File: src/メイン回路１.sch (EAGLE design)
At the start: 33 parts, among them T1 一般的なトランジスタ, T2 一般的なトランジスタ, T3 一般的なトランジスタ, T4 一般的なトランジスタ

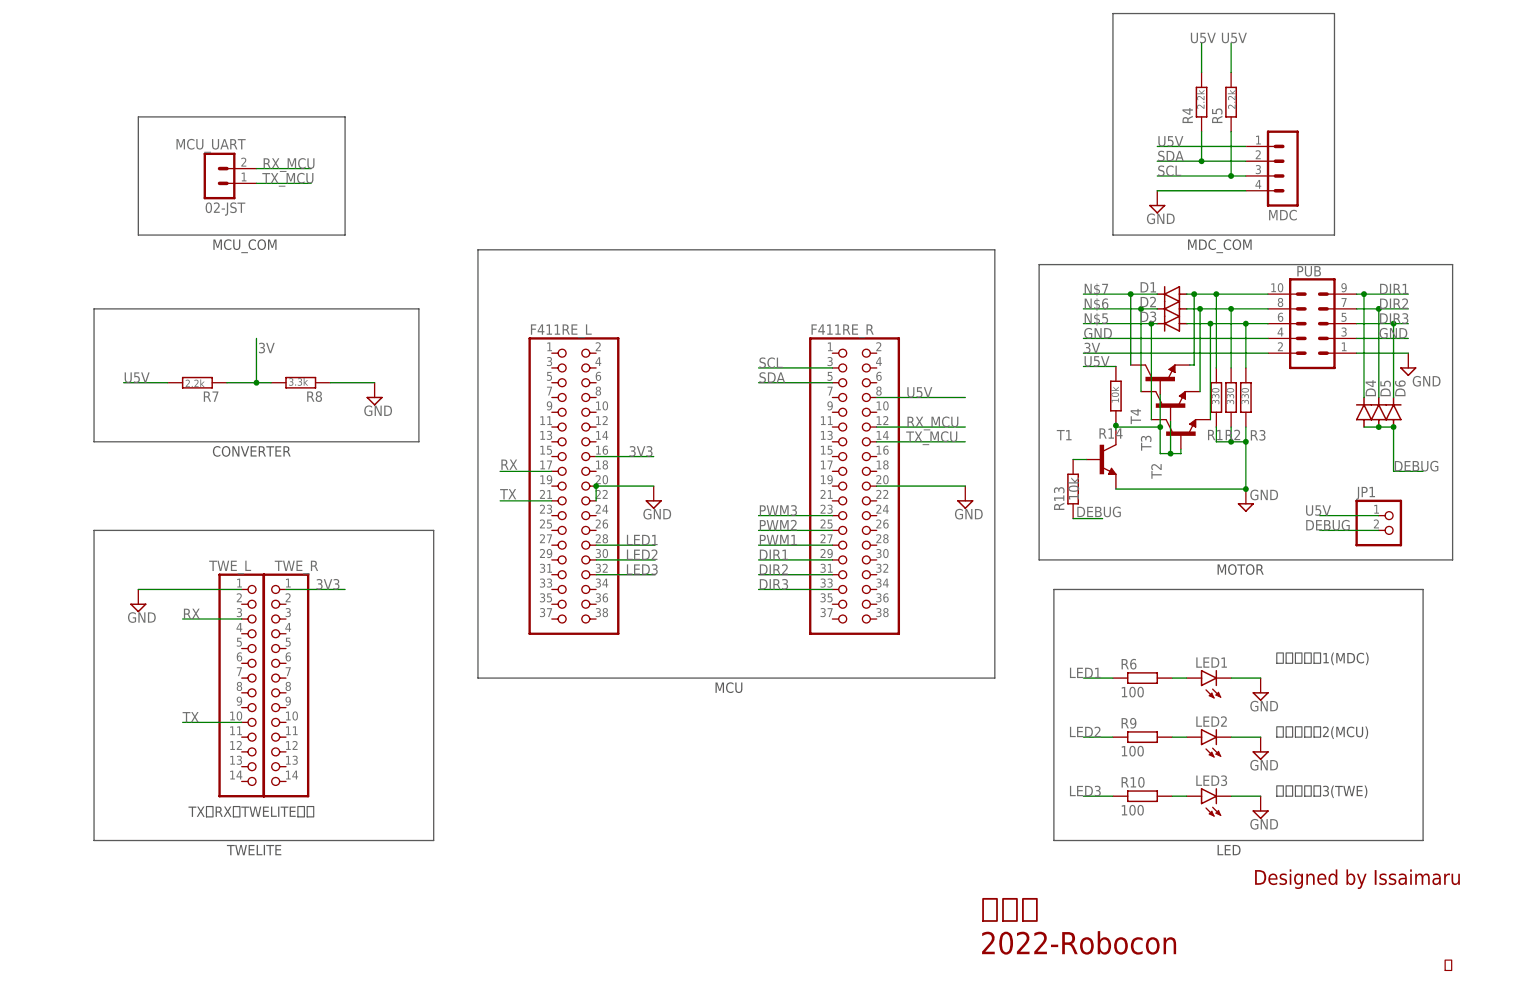
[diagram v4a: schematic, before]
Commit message: [add]メイン回路1にソケット置きを追加
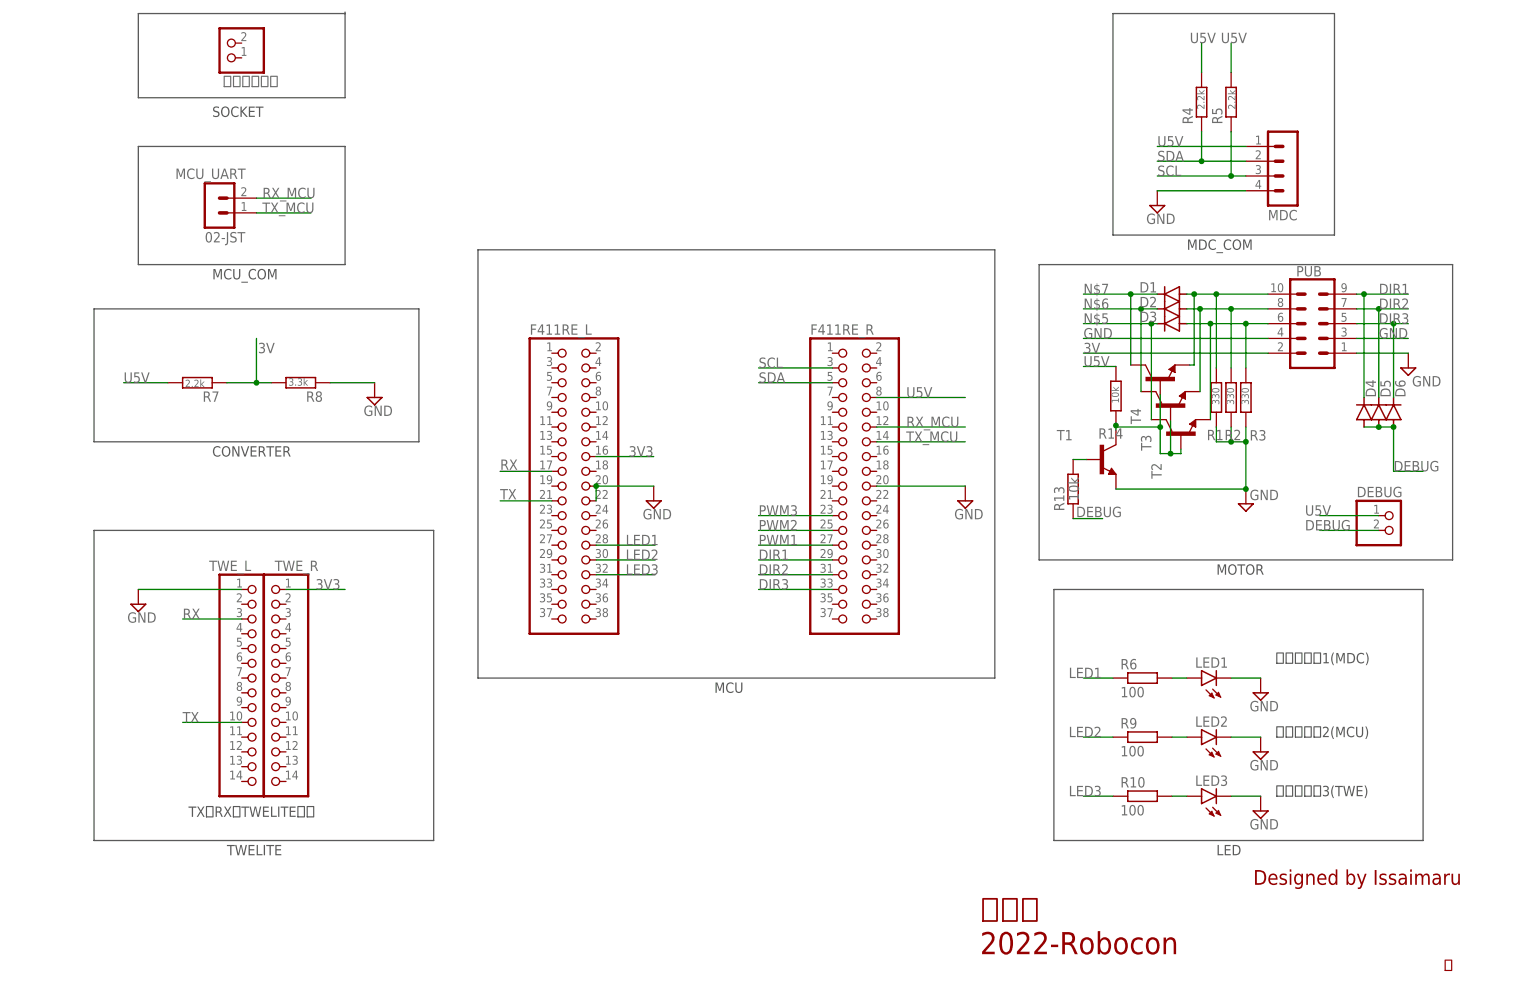
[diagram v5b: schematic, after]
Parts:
- added ソケット置き: (no value), pinhead:PINHD-1X2
- renumbered JP1 to DEBUG
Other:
- note added: "SOCKET"
- moved on the sheet: MCU_UART
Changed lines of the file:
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@@
 <part name="LED3" library="led" library_urn="urn:adsk.eagle:library:259" deviceset="LED" device="5MM" package3d_urn="urn:adsk.eagle:package:15799/2"/>
 <part name="SUPPLY10" library="supply2" library_urn="urn:adsk.eagle:library:372" deviceset="GND" device=""/>
-<part name="JP1" library="pinhead" library_urn="urn:adsk.eagle:library:325" deviceset="PINHD-1X2" device="" package3d_urn="urn:adsk.eagle:package:22435/2"/>
+<part name="DEBUG" library="pinhead" library_urn="urn:adsk.eagle:library:325" deviceset="PINHD-1X2" device="" package3d_urn="urn:adsk.eagle:package:22435/2"/>
 <part name="R13" library="rcl" library_urn="urn:adsk.eagle:library:334" deviceset="R-EU_" device="0204/7" package3d_urn="urn:adsk.eagle:package:23498/2" value="10k"/>
 <part name="D1" library="diode" library_urn="urn:adsk.eagle:library:210" deviceset="1N4004" device="" package3d_urn="urn:adsk.eagle:package:43336/1"/>
@@
 <part name="T3" library="一般的なトランジスタ" deviceset="一般的なトランジスタ" device=""/>
 <part name="T4" library="一般的なトランジスタ" deviceset="一般的なトランジスタ" device=""/>
+<part name="ソケット置き" library="pinhead" library_urn="urn:adsk.eagle:library:325" deviceset="PINHD-1X2" device="" package3d_urn="urn:adsk.eagle:package:22435/2"/>
 </parts>
 <sheets>
@@
 <wire x1="73.66" y1="96.52" x2="73.66" y2="119.38" width="0.1524" layer="97"/>
 <wire x1="73.66" y1="119.38" x2="17.78" y2="119.38" width="0.1524" layer="97"/>
-<wire x1="25.4" y1="152.4" x2="25.4" y2="132.08" width="0.1524" layer="97"/>
-<wire x1="25.4" y1="132.08" x2="60.96" y2="132.08" width="0.1524" layer="97"/>
-<wire x1="60.96" y1="132.08" x2="60.96" y2="152.4" width="0.1524" layer="97"/>
-<wire x1="60.96" y1="152.4" x2="25.4" y2="152.4" width="0.1524" layer="97"/>
+<wire x1="25.4" y1="147.32" x2="25.4" y2="127" width="0.1524" layer="97"/>
+<wire x1="25.4" y1="127" x2="60.96" y2="127" width="0.1524" layer="97"/>
+<wire x1="60.96" y1="127" x2="60.96" y2="147.32" width="0.1524" layer="97"/>
+<wire x1="60.96" y1="147.32" x2="25.4" y2="147.32" width="0.1524" layer="97"/>
 <wire x1="83.82" y1="129.54" x2="83.82" y2="55.88" width="0.1524" layer="97"/>
 <wire x1="83.82" y1="55.88" x2="172.72" y2="55.88" width="0.1524" layer="97"/>
@@
 <wire x1="246.38" y1="27.94" x2="246.38" y2="71.12" width="0.1524" layer="97"/>
 <wire x1="246.38" y1="71.12" x2="182.88" y2="71.12" width="0.1524" layer="97"/>
-<text x="38.1" y="129.54" size="1.778" layer="97">MCU_COM</text>
+<text x="38.1" y="124.46" size="1.778" layer="97">MCU_COM</text>
 <text x="38.1" y="93.98" size="1.778" layer="97">CONVERTER</text>
 <text x="40.64" y="25.4" size="1.778" layer="97">TWELITE</text>
@@
 <text x="210.82" y="73.66" size="1.778" layer="97">MOTOR</text>
 <text x="210.82" y="25.4" size="1.778" layer="97">LED</text>
+<wire x1="25.4" y1="170.18" x2="25.4" y2="155.702" width="0.1524" layer="97"/>
+<wire x1="25.4" y1="155.702" x2="60.96" y2="155.702" width="0.1524" layer="97"/>
+<wire x1="60.96" y1="155.702" x2="60.96" y2="170.18" width="0.1524" layer="97"/>
+<wire x1="60.96" y1="170.434" x2="60.96" y2="170.18" width="0.1524" layer="97"/>
+<wire x1="60.96" y1="170.18" x2="25.4" y2="170.18" width="0.1524" layer="97"/>
+<text x="38.1" y="152.4" size="1.778" layer="97">SOCKET</text>
 </plain>
 <instances>
@@
 <attribute name="NAME" x="224.536" y="124.968" size="1.778" layer="95"/>
 </instance>
-<instance part="MCU_UART" gate="G$1" x="38.1" y="143.51" smashed="yes">
-<attribute name="VALUE" x="36.83" y="135.89" size="1.778" layer="96"/>
-<attribute name="NAME" x="31.75" y="146.812" size="1.778" layer="95"/>
+<instance part="MCU_UART" gate="G$1" x="38.1" y="138.43" smashed="yes">
+<attribute name="VALUE" x="36.83" y="130.81" size="1.778" layer="96"/>
+<attribute name="NAME" x="31.75" y="141.732" size="1.778" layer="95"/>
 </instance>
 <instance part="FRAME1" gate="G$1" x="0" y="0" smashed="yes">
@@
 <attribute name="VALUE" x="216.535" y="29.845" size="1.778" layer="96"/>
 </instance>
-<instance part="JP1" gate="G$1" x="241.3" y="81.28" smashed="yes">
+<instance part="DEBUG" gate="G$1" x="241.3" y="81.28" smashed="yes">
 <attribute name="NAME" x="234.95" y="86.995" size="1.778" layer="95"/>
 <attribute name="VALUE" x="234.95" y="76.2" size="1.778" layer="96"/>
@@
 <instance part="T4" gate="G$1" x="201.168" y="107.188" smashed="yes" rot="R90">
 <attribute name="NAME" x="197.866" y="99.568" size="1.778" layer="95" rot="R90"/>
+</instance>
+<instance part="ソケット置き" gate="G$1" x="40.64" y="165.1" smashed="yes" rot="R180">
+<attribute name="NAME" x="49.53" y="159.385" size="1.778" layer="95" rot="R180"/>
+<attribute name="VALUE" x="46.99" y="170.18" size="1.778" layer="96" rot="R180"/>
 </instance>
 </instances>
@@
 <segment>
 <pinref part="MCU_UART" gate="G$1" pin="2"/>
-<wire x1="45.72" y1="143.51" x2="55.118" y2="143.51" width="0.1524" layer="91"/>
-<label x="46.736" y="143.51" size="1.778" layer="95"/>
+<wire x1="45.72" y1="138.43" x2="55.118" y2="138.43" width="0.1524" layer="91"/>
+<label x="46.736" y="138.43" size="1.778" layer="95"/>
 </segment>
 <segment>
@@
 <segment>
 <pinref part="MCU_UART" gate="G$1" pin="1"/>
-<wire x1="45.72" y1="140.97" x2="55.118" y2="140.97" width="0.1524" layer="91"/>
-<label x="46.736" y="140.97" size="1.778" layer="95"/>
+<wire x1="45.72" y1="135.89" x2="55.118" y2="135.89" width="0.1524" layer="91"/>
+<label x="46.736" y="135.89" size="1.778" layer="95"/>
 </segment>
 <segment>
@@
 </segment>
 <segment>
-<pinref part="JP1" gate="G$1" pin="1"/>
+<pinref part="DEBUG" gate="G$1" pin="1"/>
 <wire x1="238.76" y1="83.82" x2="228.6" y2="83.82" width="0.1524" layer="91"/>
 <label x="226.06" y="83.82" size="1.778" layer="95"/>
@@
 <net name="DEBUG" class="0">
 <segment>
-<pinref part="JP1" gate="G$1" pin="2"/>
+<pinref part="DEBUG" gate="G$1" pin="2"/>
 <wire x1="238.76" y1="81.28" x2="228.6" y2="81.28" width="0.1524" layer="91"/>
 <label x="226.06" y="81.28" size="1.778" layer="95"/>

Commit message: [fix]接続問題の解消
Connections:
- removed net N$5: D3.C, T2.C
- removed net N$6: D2.C, T3.C
- removed net N$7: D1.C, T4.C
- new net N$8: D1.A, PUB.10, R1.2, T4.E
- new net N$9: D2.A, PUB.8, R2.2, T3.E
- new net N$Q0: D3.A, PUB.6, R3.2, T2.E
- net PWM1: now also D1.C, T4.C; no longer D1.A, PUB.10, R1.2, T4.E
- net PWM2: now also D2.C, T3.C; no longer D2.A, PUB.8, R2.2, T3.E
- net PWM3: now also D3.C, T2.C; no longer D3.A, PUB.6, R3.2, T2.E
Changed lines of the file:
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@@
 <net name="PWM2" class="0">
-<segment>
-<pinref part="PUB" gate="G$1" pin="8"/>
-<wire x1="219.71" y1="119.38" x2="213.36" y2="119.38" width="0.1524" layer="91"/>
-<wire x1="213.36" y1="119.38" x2="213.36" y2="109.22" width="0.1524" layer="91"/>
-<junction x="213.36" y="119.38"/>
-<pinref part="R2" gate="G$1" pin="2"/>
-<wire x1="213.36" y1="119.38" x2="208.026" y2="119.38" width="0.1524" layer="91"/>
-<pinref part="D2" gate="1" pin="A"/>
-<wire x1="208.026" y1="119.38" x2="205.74" y2="119.38" width="0.1524" layer="91"/>
-<wire x1="208.026" y1="105.156" x2="208.026" y2="119.38" width="0.1524" layer="91"/>
-<junction x="208.026" y="119.38"/>
-<pinref part="T3" gate="G$1" pin="E"/>
-</segment>
 <segment>
 <pinref part="F411RE_R" gate="G$1" pin="25"/>
@@
 <label x="132.08" y="81.28" size="1.778" layer="95"/>
 </segment>
+<segment>
+<label x="187.96" y="119.38" size="1.778" layer="95"/>
+<pinref part="D2" gate="1" pin="C"/>
+<wire x1="200.66" y1="119.38" x2="197.866" y2="119.38" width="0.1524" layer="91"/>
+<pinref part="T3" gate="G$1" pin="C"/>
+<wire x1="197.866" y1="119.38" x2="187.96" y2="119.38" width="0.1524" layer="91"/>
+<wire x1="197.866" y1="105.156" x2="197.866" y2="119.38" width="0.1524" layer="91"/>
+<junction x="197.866" y="119.38"/>
+</segment>
 </net>
 <net name="PWM3" class="0">
-<segment>
-<pinref part="PUB" gate="G$1" pin="6"/>
-<wire x1="219.71" y1="116.84" x2="215.9" y2="116.84" width="0.1524" layer="91"/>
-<wire x1="215.9" y1="109.22" x2="215.9" y2="116.84" width="0.1524" layer="91"/>
-<junction x="215.9" y="116.84"/>
-<pinref part="R3" gate="G$1" pin="2"/>
-<wire x1="215.9" y1="116.84" x2="209.804" y2="116.84" width="0.1524" layer="91"/>
-<pinref part="D3" gate="1" pin="A"/>
-<wire x1="209.804" y1="116.84" x2="205.74" y2="116.84" width="0.1524" layer="91"/>
-<wire x1="209.804" y1="100.33" x2="209.804" y2="116.84" width="0.1524" layer="91"/>
-<junction x="209.804" y="116.84"/>
-<pinref part="T2" gate="G$1" pin="E"/>
-</segment>
 <segment>
 <pinref part="F411RE_R" gate="G$1" pin="23"/>
 <wire x1="144.78" y1="83.82" x2="132.08" y2="83.82" width="0.1524" layer="91"/>
 <label x="132.08" y="83.82" size="1.778" layer="95"/>
+</segment>
+<segment>
+<label x="187.96" y="116.84" size="1.778" layer="95"/>
+<pinref part="D3" gate="1" pin="C"/>
+<wire x1="200.66" y1="116.84" x2="199.644" y2="116.84" width="0.1524" layer="91"/>
+<pinref part="T2" gate="G$1" pin="C"/>
+<wire x1="199.644" y1="116.84" x2="187.96" y2="116.84" width="0.1524" layer="91"/>
+<wire x1="199.644" y1="100.33" x2="199.644" y2="116.84" width="0.1524" layer="91"/>
+<junction x="199.644" y="116.84"/>
 </segment>
 </net>
@@
 <net name="PWM1" class="0">
 <segment>
-<pinref part="D1" gate="1" pin="A"/>
-<pinref part="PUB" gate="G$1" pin="10"/>
-<wire x1="219.71" y1="121.92" x2="210.82" y2="121.92" width="0.1524" layer="91"/>
-<pinref part="R1" gate="G$1" pin="2"/>
-<wire x1="210.82" y1="121.92" x2="207.01" y2="121.92" width="0.1524" layer="91"/>
-<wire x1="207.01" y1="121.92" x2="205.74" y2="121.92" width="0.1524" layer="91"/>
-<wire x1="210.82" y1="109.22" x2="210.82" y2="121.92" width="0.1524" layer="91"/>
-<junction x="210.82" y="121.92"/>
-<pinref part="T4" gate="G$1" pin="E"/>
-<wire x1="206.248" y1="109.728" x2="207.01" y2="109.728" width="0.1524" layer="91"/>
-<wire x1="207.01" y1="109.728" x2="207.01" y2="121.92" width="0.1524" layer="91"/>
-<junction x="207.01" y="121.92"/>
-</segment>
-<segment>
 <pinref part="F411RE_R" gate="G$1" pin="27"/>
 <wire x1="144.78" y1="78.74" x2="132.08" y2="78.74" width="0.1524" layer="91"/>
 <label x="132.08" y="78.74" size="1.778" layer="95"/>
+</segment>
+<segment>
+<label x="187.96" y="121.92" size="1.778" layer="95"/>
+<pinref part="D1" gate="1" pin="C"/>
+<wire x1="200.66" y1="121.92" x2="196.088" y2="121.92" width="0.1524" layer="91"/>
+<pinref part="T4" gate="G$1" pin="C"/>
+<wire x1="196.088" y1="121.92" x2="187.96" y2="121.92" width="0.1524" layer="91"/>
+<wire x1="196.088" y1="109.728" x2="196.088" y2="121.92" width="0.1524" layer="91"/>
+<junction x="196.088" y="121.92"/>
 </segment>
 </net>
@@
 </segment>
 </net>
-<net name="N$5" class="0">
-<segment>
-<label x="187.96" y="116.84" size="1.778" layer="95"/>
-<pinref part="D3" gate="1" pin="C"/>
-<wire x1="200.66" y1="116.84" x2="199.644" y2="116.84" width="0.1524" layer="91"/>
-<pinref part="T2" gate="G$1" pin="C"/>
-<wire x1="199.644" y1="116.84" x2="187.96" y2="116.84" width="0.1524" layer="91"/>
-<wire x1="199.644" y1="100.33" x2="199.644" y2="116.84" width="0.1524" layer="91"/>
-<junction x="199.644" y="116.84"/>
-</segment>
-</net>
-<net name="N$6" class="0">
-<segment>
-<label x="187.96" y="119.38" size="1.778" layer="95"/>
-<pinref part="D2" gate="1" pin="C"/>
-<wire x1="200.66" y1="119.38" x2="197.866" y2="119.38" width="0.1524" layer="91"/>
-<pinref part="T3" gate="G$1" pin="C"/>
-<wire x1="197.866" y1="119.38" x2="187.96" y2="119.38" width="0.1524" layer="91"/>
-<wire x1="197.866" y1="105.156" x2="197.866" y2="119.38" width="0.1524" layer="91"/>
-<junction x="197.866" y="119.38"/>
-</segment>
-</net>
-<net name="N$7" class="0">
-<segment>
-<label x="187.96" y="121.92" size="1.778" layer="95"/>
-<pinref part="D1" gate="1" pin="C"/>
-<wire x1="200.66" y1="121.92" x2="196.088" y2="121.92" width="0.1524" layer="91"/>
-<pinref part="T4" gate="G$1" pin="C"/>
-<wire x1="196.088" y1="121.92" x2="187.96" y2="121.92" width="0.1524" layer="91"/>
-<wire x1="196.088" y1="109.728" x2="196.088" y2="121.92" width="0.1524" layer="91"/>
-<junction x="196.088" y="121.92"/>
-</segment>
-</net>
+<net name="N$8" class="0">
+<segment>
+<pinref part="D1" gate="1" pin="A"/>
+<pinref part="PUB" gate="G$1" pin="10"/>
+<wire x1="219.71" y1="121.92" x2="210.82" y2="121.92" width="0.1524" layer="91"/>
+<pinref part="R1" gate="G$1" pin="2"/>
+<wire x1="210.82" y1="121.92" x2="207.01" y2="121.92" width="0.1524" layer="91"/>
+<wire x1="207.01" y1="121.92" x2="205.74" y2="121.92" width="0.1524" layer="91"/>
+<wire x1="210.82" y1="109.22" x2="210.82" y2="121.92" width="0.1524" layer="91"/>
+<junction x="210.82" y="121.92"/>
+<pinref part="T4" gate="G$1" pin="E"/>
+<wire x1="206.248" y1="109.728" x2="207.01" y2="109.728" width="0.1524" layer="91"/>
+<wire x1="207.01" y1="109.728" x2="207.01" y2="121.92" width="0.1524" layer="91"/>
+<junction x="207.01" y="121.92"/>
+</segment>
+</net>
+<net name="N$9" class="0">
+<segment>
+<pinref part="PUB" gate="G$1" pin="8"/>
+<wire x1="219.71" y1="119.38" x2="213.36" y2="119.38" width="0.1524" layer="91"/>
+<wire x1="213.36" y1="119.38" x2="213.36" y2="109.22" width="0.1524" layer="91"/>
+<junction x="213.36" y="119.38"/>
+<pinref part="R2" gate="G$1" pin="2"/>
+<wire x1="213.36" y1="119.38" x2="208.026" y2="119.38" width="0.1524" layer="91"/>
+<pinref part="D2" gate="1" pin="A"/>
+<wire x1="208.026" y1="119.38" x2="205.74" y2="119.38" width="0.1524" layer="91"/>
+<wire x1="208.026" y1="105.156" x2="208.026" y2="119.38" width="0.1524" layer="91"/>
+<junction x="208.026" y="119.38"/>
+<pinref part="T3" gate="G$1" pin="E"/>
+</segment>
+</net>
+<net name="N$Q0" class="0">
+<segment>
+<pinref part="PUB" gate="G$1" pin="6"/>
+<wire x1="219.71" y1="116.84" x2="215.9" y2="116.84" width="0.1524" layer="91"/>
+<wire x1="215.9" y1="109.22" x2="215.9" y2="116.84" width="0.1524" layer="91"/>
+<junction x="215.9" y="116.84"/>
+<pinref part="R3" gate="G$1" pin="2"/>
+<wire x1="215.9" y1="116.84" x2="209.804" y2="116.84" width="0.1524" layer="91"/>
+<pinref part="D3" gate="1" pin="A"/>
+<wire x1="209.804" y1="116.84" x2="205.74" y2="116.84" width="0.1524" layer="91"/>
+<wire x1="209.804" y1="100.33" x2="209.804" y2="116.84" width="0.1524" layer="91"/>
+<junction x="209.804" y="116.84"/>
+<pinref part="T2" gate="G$1" pin="E"/>
+</segment>
+</net>
